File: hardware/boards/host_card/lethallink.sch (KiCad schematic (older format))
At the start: 11 parts, among them J1 PCIe-x4

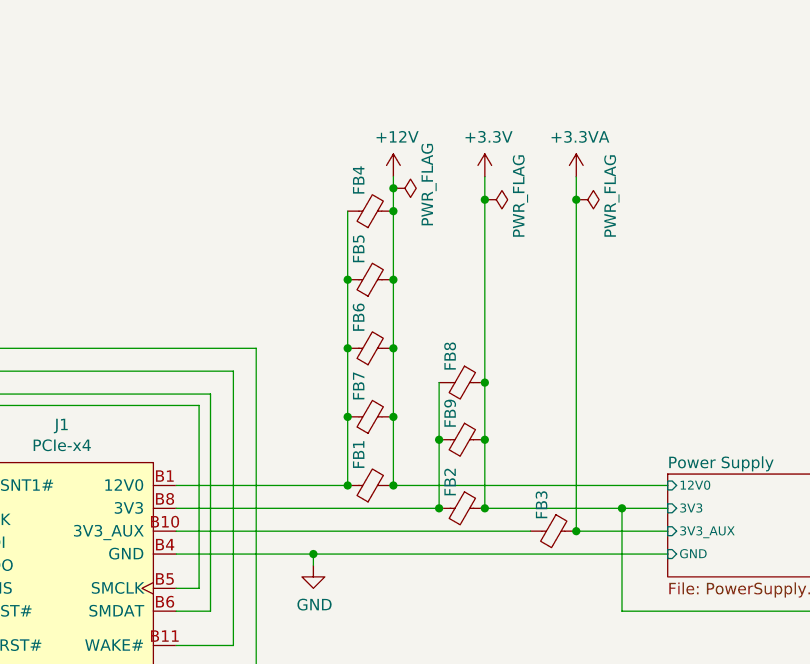
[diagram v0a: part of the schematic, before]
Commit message: Re-routed the PCIe power input side of things to make it not such a massive mess
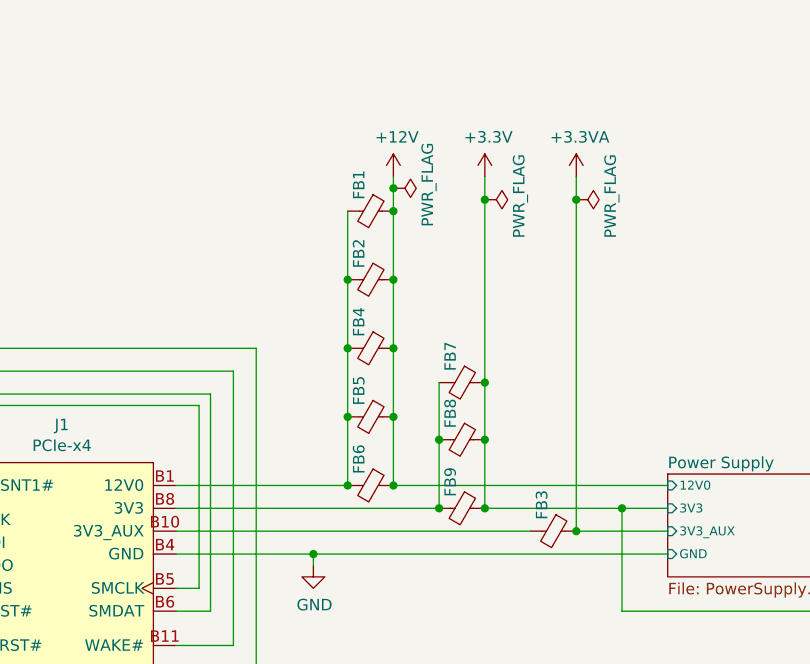
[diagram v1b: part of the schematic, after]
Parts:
- FB1, FB4, FB5, FB6, FB7: value 100 @ 100MHz -> 33 @ 100Mhz; footprint Resistor_SMD:R_0603_1608Metric -> Resistor_SMD:R_0402_1005Metric; MPN BLM18KG101TN1D -> BLM15PX330SN1D
- FB2, FB3, FB8, FB9: value 220 @ 100Mhz -> 33 @ 100Mhz; footprint Resistor_SMD:R_0603_1608Metric -> Resistor_SMD:R_0402_1005Metric; MPN BLM18AG221SN1D -> BLM15PX330SN1D
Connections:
- net +12V: now also FB1.1, FB2.1, FB4.1, FB5.1, FB6.1; no longer FB1.2, FB4.2, FB5.2, FB6.2, FB7.2
- net +3V3: now also FB7.1; no longer FB2.1
- net at FB8.2, FB9.2, J1.A10 (3V3)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: now also FB7.2; no longer FB2.2
- net at J1.A2 (12V0), J1.A3 (12V0), J1.B1 (12V0)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: now also FB1.2, FB2.2, FB4.2, FB5.2, FB6.2; no longer FB1.1, FB4.1, FB5.1, FB6.1, FB7.1
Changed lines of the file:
@@
 Wire Wire Line
 	4300 4350 5850 4350
-Connection ~ 5450 4250
 Wire Wire Line
 	4650 4050 5850 4050
@@
 F7 "VBUS" I R 9000 4050 39
 $EndSheet
-$Comp
-L Device:Ferrite_Bead_Small FB3
-U 1 1 5F57A174
-P 5350 4250
-F 0 "FB3" H 5300 4200 50  0000 R CNN
-F 1 "220 @ 100Mhz" H 5500 4450 50  0001 R CNN
-F 2 "Resistor_SMD:R_0603_1608Metric" V 5280 4250 50  0001 C CNN
-F 3 "~" H 5350 4250 50  0001 C CNN
-F 4 "Murata Electronics" H 5350 4250 50  0001 C CNN "MFR"
-F 5 "BLM18AG221SN1D" H 5350 4250 50  0001 C CNN "MPN"
-	1    5350 4250
-	0    1    1    0
-$EndComp
-$Comp
-L Device:Ferrite_Bead_Small FB2
-U 1 1 5F579DEB
-P 4950 4150
-F 0 "FB2" H 4900 4100 50  0000 R CNN
-F 1 "220 @ 100Mhz" H 5100 4350 50  0001 R CNN
-F 2 "Resistor_SMD:R_0603_1608Metric" V 4880 4150 50  0001 C CNN
-F 3 "~" H 4950 4150 50  0001 C CNN
-F 4 "Murata Electronics" H 4950 4150 50  0001 C CNN "MFR"
-F 5 "BLM18AG221SN1D" H 4950 4150 50  0001 C CNN "MPN"
-	1    4950 4150
-	0    1    1    0
-$EndComp
 Wire Wire Line
 	5650 4150 5850 4150
@@
 Wire Wire Line
 	7000 4050 8350 4050
-$Comp
-L Device:Ferrite_Bead_Small FB1
-U 1 1 5EEA5842
-P 4550 4050
-F 0 "FB1" H 4750 4100 50  0000 R CNN
-F 1 "100 @ 100MHz" H 4700 4250 50  0001 R CNN
-F 2 "Resistor_SMD:R_0603_1608Metric" V 4480 4050 50  0001 C CNN
-F 3 "~" H 4550 4050 50  0001 C CNN
-F 4 "Murata Electronics" H 4550 4050 50  0001 C CNN "MFR"
-F 5 "BLM18KG101TN1D" H 4550 4050 50  0001 C CNN "MPN"
-	1    4550 4050
-	0    -1   -1   0
-$EndComp
 $Sheet
 S 5850 4000 950  450
@@
 $EndComp
 Connection ~ 4300 4350
-$Comp
-L Device:Ferrite_Bead_Small FB9
-U 1 1 5F410C07
-P 4950 3850
-F 0 "FB9" H 4900 3800 50  0000 R CNN
-F 1 "220 @ 100Mhz" H 5100 4050 50  0001 R CNN
-F 2 "Resistor_SMD:R_0603_1608Metric" V 4880 3850 50  0001 C CNN
-F 3 "~" H 4950 3850 50  0001 C CNN
-F 4 "Murata Electronics" H 4950 3850 50  0001 C CNN "MFR"
-F 5 "BLM18AG221SN1D" H 4950 3850 50  0001 C CNN "MPN"
-	1    4950 3850
-	0    1    1    0
-$EndComp
-Connection ~ 5050 3850
-Wire Wire Line
-	5050 3850 5050 4150
-Connection ~ 5050 4150
-$Comp
-L Device:Ferrite_Bead_Small FB8
-U 1 1 5F41D475
-P 4950 3600
-F 0 "FB8" H 4900 3550 50  0000 R CNN
-F 1 "220 @ 100Mhz" H 5100 3800 50  0001 R CNN
-F 2 "Resistor_SMD:R_0603_1608Metric" V 4880 3600 50  0001 C CNN
-F 3 "~" H 4950 3600 50  0001 C CNN
-F 4 "Murata Electronics" H 4950 3600 50  0001 C CNN "MFR"
-F 5 "BLM18AG221SN1D" H 4950 3600 50  0001 C CNN "MPN"
-	1    4950 3600
-	0    1    1    0
-$EndComp
-Connection ~ 5050 3600
-Wire Wire Line
-	5050 3600 5050 3850
 Wire Wire Line
 	5450 2700 5450 2800
-Connection ~ 4650 4050
-$Comp
-L Device:Ferrite_Bead_Small FB7
-U 1 1 5F46A338
-P 4550 3750
-F 0 "FB7" H 4750 3800 50  0000 R CNN
-F 1 "100 @ 100MHz" H 4700 3950 50  0001 R CNN
-F 2 "Resistor_SMD:R_0603_1608Metric" V 4480 3750 50  0001 C CNN
-F 3 "~" H 4550 3750 50  0001 C CNN
-F 4 "Murata Electronics" H 4550 3750 50  0001 C CNN "MFR"
-F 5 "BLM18KG101TN1D" H 4550 3750 50  0001 C CNN "MPN"
-	1    4550 3750
-	0    -1   -1   0
-$EndComp
-Connection ~ 4650 3750
-Wire Wire Line
-	4650 3750 4650 4050
-$Comp
-L Device:Ferrite_Bead_Small FB6
-U 1 1 5F46A91E
-P 4550 3450
-F 0 "FB6" H 4750 3500 50  0000 R CNN
-F 1 "100 @ 100MHz" H 4700 3650 50  0001 R CNN
-F 2 "Resistor_SMD:R_0603_1608Metric" V 4480 3450 50  0001 C CNN
-F 3 "~" H 4550 3450 50  0001 C CNN
-F 4 "Murata Electronics" H 4550 3450 50  0001 C CNN "MFR"
-F 5 "BLM18KG101TN1D" H 4550 3450 50  0001 C CNN "MPN"
-	1    4550 3450
-	0    -1   -1   0
-$EndComp
-Connection ~ 4650 3450
-Wire Wire Line
-	4650 3450 4650 3750
-$Comp
-L Device:Ferrite_Bead_Small FB5
-U 1 1 5F4730D6
-P 4550 3150
-F 0 "FB5" H 4750 3200 50  0000 R CNN
-F 1 "100 @ 100MHz" H 4700 3350 50  0001 R CNN
-F 2 "Resistor_SMD:R_0603_1608Metric" V 4480 3150 50  0001 C CNN
-F 3 "~" H 4550 3150 50  0001 C CNN
-F 4 "Murata Electronics" H 4550 3150 50  0001 C CNN "MFR"
-F 5 "BLM18KG101TN1D" H 4550 3150 50  0001 C CNN "MPN"
-	1    4550 3150
-	0    -1   -1   0
-$EndComp
-Connection ~ 4650 3150
-Wire Wire Line
-	4650 3150 4650 3450
-$Comp
-L Device:Ferrite_Bead_Small FB4
-U 1 1 5F479C67
-P 4550 2850
-F 0 "FB4" H 4750 2900 50  0000 R CNN
-F 1 "100 @ 100MHz" H 4700 3050 50  0001 R CNN
-F 2 "Resistor_SMD:R_0603_1608Metric" V 4480 2850 50  0001 C CNN
-F 3 "~" H 4550 2850 50  0001 C CNN
-F 4 "Murata Electronics" H 4550 2850 50  0001 C CNN "MFR"
-F 5 "BLM18KG101TN1D" H 4550 2850 50  0001 C CNN "MPN"
-	1    4550 2850
-	0    -1   -1   0
-$EndComp
-Connection ~ 4650 2850
-Wire Wire Line
-	4650 2850 4650 3150
-Wire Wire Line
-	4450 2850 4450 3150
-Wire Wire Line
-	4450 3450 4450 3750
-Wire Wire Line
-	4450 3150 4450 3450
-Connection ~ 4450 3150
-Connection ~ 4450 3450
-Wire Wire Line
-	4450 3750 4450 4050
-Connection ~ 4450 3750
-Connection ~ 4450 4050
-Wire Wire Line
-	4850 3600 4850 3850
-Wire Wire Line
-	4850 3850 4850 4150
-Connection ~ 4850 3850
-Connection ~ 4850 4150
 $Comp
 L Device:Ferrite_Bead_Small FB10
@@
 $EndComp
 Connection ~ 4650 2750
-Wire Wire Line
-	4650 2750 4650 2850
 $Comp
 L power:PWR_FLAG #FLG0102
@@
 $EndComp
 Connection ~ 5050 2800
-Wire Wire Line
-	5050 2800 5050 3600
 $Comp
 L power:PWR_FLAG #FLG0103
@@
 Wire Wire Line
 	9900 2700 10050 2700
+Wire Wire Line
+	4450 2850 4450 3150
+Wire Wire Line
+	4650 2750 4650 2850
+Wire Wire Line
+	4850 3600 4850 3850
+Wire Wire Line
+	5050 2800 5050 3600
+Connection ~ 5450 4250
+$Comp
+L Device:Ferrite_Bead_Small FB3
+U 1 1 5F57A174
+P 5350 4250
+F 0 "FB3" H 5300 4200 50  0000 R CNN
+F 1 "33 @ 100Mhz" H 5500 4450 50  0001 R CNN
+F 2 "Resistor_SMD:R_0402_1005Metric" V 5280 4250 50  0001 C CNN
+F 3 "~" H 5350 4250 50  0001 C CNN
+F 4 "Murata Electronics" H 5350 4250 50  0001 C CNN "MFR"
+F 5 "BLM15PX330SN1D" H 5350 4250 50  0001 C CNN "MPN"
+	1    5350 4250
+	0    1    1    0
+$EndComp
+$Comp
+L Device:Ferrite_Bead_Small FB9
+U 1 1 5EFC20C8
+P 4950 4150
+F 0 "FB9" H 4900 4100 50  0000 R CNN
+F 1 "33 @ 100Mhz" H 5100 4350 50  0001 R CNN
+F 2 "Resistor_SMD:R_0402_1005Metric" V 4880 4150 50  0001 C CNN
+F 3 "~" H 4950 4150 50  0001 C CNN
+F 4 "Murata Electronics" H 4950 4150 50  0001 C CNN "MFR"
+F 5 "BLM15PX330SN1D" H 4950 4150 50  0001 C CNN "MPN"
+	1    4950 4150
+	0    1    1    0
+$EndComp
+Connection ~ 5050 4150
+Connection ~ 4850 4150
+$Comp
+L Device:Ferrite_Bead_Small FB7
+U 1 1 5EFC24FC
+P 4950 3600
+F 0 "FB7" H 4900 3550 50  0000 R CNN
+F 1 "33 @ 100Mhz" H 5100 3800 50  0001 R CNN
+F 2 "Resistor_SMD:R_0402_1005Metric" V 4880 3600 50  0001 C CNN
+F 3 "~" H 4950 3600 50  0001 C CNN
+F 4 "Murata Electronics" H 4950 3600 50  0001 C CNN "MFR"
+F 5 "BLM15PX330SN1D" H 4950 3600 50  0001 C CNN "MPN"
+	1    4950 3600
+	0    1    1    0
+$EndComp
+Connection ~ 5050 3600
+Wire Wire Line
+	5050 3600 5050 3850
+$Comp
+L Device:Ferrite_Bead_Small FB8
+U 1 1 5EFC3129
+P 4950 3850
+F 0 "FB8" H 4900 3800 50  0000 R CNN
+F 1 "33 @ 100Mhz" H 5100 4050 50  0001 R CNN
+F 2 "Resistor_SMD:R_0402_1005Metric" V 4880 3850 50  0001 C CNN
+F 3 "~" H 4950 3850 50  0001 C CNN
+F 4 "Murata Electronics" H 4950 3850 50  0001 C CNN "MFR"
+F 5 "BLM15PX330SN1D" H 4950 3850 50  0001 C CNN "MPN"
+	1    4950 3850
+	0    1    1    0
+$EndComp
+Connection ~ 5050 3850
+Wire Wire Line
+	5050 3850 5050 4150
+Connection ~ 4850 3850
+Wire Wire Line
+	4850 3850 4850 4150
+$Comp
+L Device:Ferrite_Bead_Small FB6
+U 1 1 5EFC353B
+P 4550 4050
+F 0 "FB6" H 4500 4000 50  0000 R CNN
+F 1 "33 @ 100Mhz" H 4700 4250 50  0001 R CNN
+F 2 "Resistor_SMD:R_0402_1005Metric" V 4480 4050 50  0001 C CNN
+F 3 "~" H 4550 4050 50  0001 C CNN
+F 4 "Murata Electronics" H 4550 4050 50  0001 C CNN "MFR"
+F 5 "BLM15PX330SN1D" H 4550 4050 50  0001 C CNN "MPN"
+	1    4550 4050
+	0    1    1    0
+$EndComp
+Connection ~ 4650 4050
+Connection ~ 4450 4050
+$Comp
+L Device:Ferrite_Bead_Small FB5
+U 1 1 5EFC39E3
+P 4550 3750
+F 0 "FB5" H 4500 3700 50  0000 R CNN
+F 1 "33 @ 100Mhz" H 4700 3950 50  0001 R CNN
+F 2 "Resistor_SMD:R_0402_1005Metric" V 4480 3750 50  0001 C CNN
+F 3 "~" H 4550 3750 50  0001 C CNN
+F 4 "Murata Electronics" H 4550 3750 50  0001 C CNN "MFR"
+F 5 "BLM15PX330SN1D" H 4550 3750 50  0001 C CNN "MPN"
+	1    4550 3750
+	0    1    1    0
+$EndComp
+Connection ~ 4650 3750
+Wire Wire Line
+	4650 3750 4650 4050
+Connection ~ 4450 3750
+Wire Wire Line
+	4450 3750 4450 4050
+$Comp
+L Device:Ferrite_Bead_Small FB4
+U 1 1 5EFC3DE1
+P 4550 3450
+F 0 "FB4" H 4500 3400 50  0000 R CNN
+F 1 "33 @ 100Mhz" H 4700 3650 50  0001 R CNN
+F 2 "Resistor_SMD:R_0402_1005Metric" V 4480 3450 50  0001 C CNN
+F 3 "~" H 4550 3450 50  0001 C CNN
+F 4 "Murata Electronics" H 4550 3450 50  0001 C CNN "MFR"
+F 5 "BLM15PX330SN1D" H 4550 3450 50  0001 C CNN "MPN"
+	1    4550 3450
+	0    1    1    0
+$EndComp
+Connection ~ 4650 3450
+Wire Wire Line
+	4650 3450 4650 3750
+Connection ~ 4450 3450
+Wire Wire Line
+	4450 3450 4450 3750
+$Comp
+L Device:Ferrite_Bead_Small FB2
+U 1 1 5EFC41A3
+P 4550 3150
+F 0 "FB2" H 4500 3100 50  0000 R CNN
+F 1 "33 @ 100Mhz" H 4700 3350 50  0001 R CNN
+F 2 "Resistor_SMD:R_0402_1005Metric" V 4480 3150 50  0001 C CNN
+F 3 "~" H 4550 3150 50  0001 C CNN
+F 4 "Murata Electronics" H 4550 3150 50  0001 C CNN "MFR"
+F 5 "BLM15PX330SN1D" H 4550 3150 50  0001 C CNN "MPN"
+	1    4550 3150
+	0    1    1    0
+$EndComp
+Connection ~ 4650 3150
+Wire Wire Line
+	4650 3150 4650 3450
+Connection ~ 4450 3150
+Wire Wire Line
+	4450 3150 4450 3450
+$Comp
+L Device:Ferrite_Bead_Small FB1
+U 1 1 5EFC45BE
+P 4550 2850
+F 0 "FB1" H 4500 2800 50  0000 R CNN
+F 1 "33 @ 100Mhz" H 4700 3050 50  0001 R CNN
+F 2 "Resistor_SMD:R_0402_1005Metric" V 4480 2850 50  0001 C CNN
+F 3 "~" H 4550 2850 50  0001 C CNN
+F 4 "Murata Electronics" H 4550 2850 50  0001 C CNN "MFR"
+F 5 "BLM15PX330SN1D" H 4550 2850 50  0001 C CNN "MPN"
+	1    4550 2850
+	0    1    1    0
+$EndComp
+Connection ~ 4650 2850
+Wire Wire Line
+	4650 2850 4650 3150
 $EndSCHEMATC

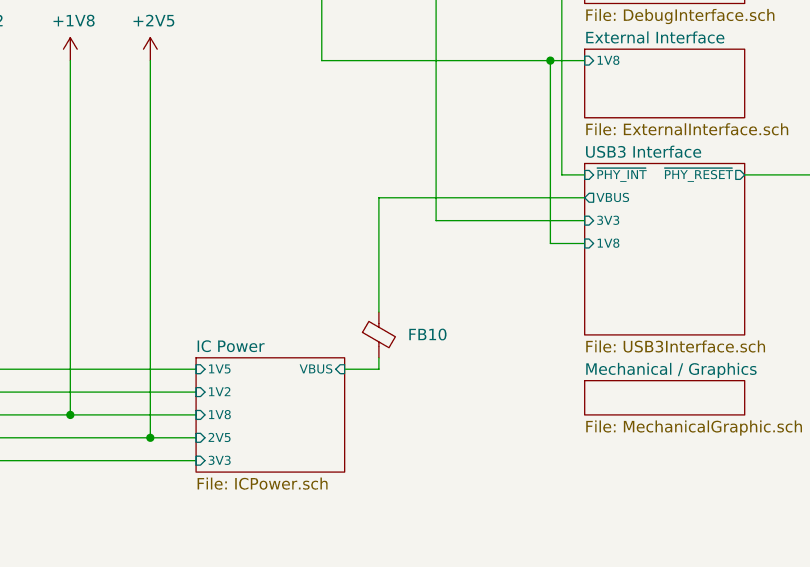
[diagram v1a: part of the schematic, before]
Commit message: Fixed up the consistancy of value naming, 100nF -> 0.1uF. Added the caps for the USB SSRX lines, moved the Ferrite for VBUS to fix a net naming issue
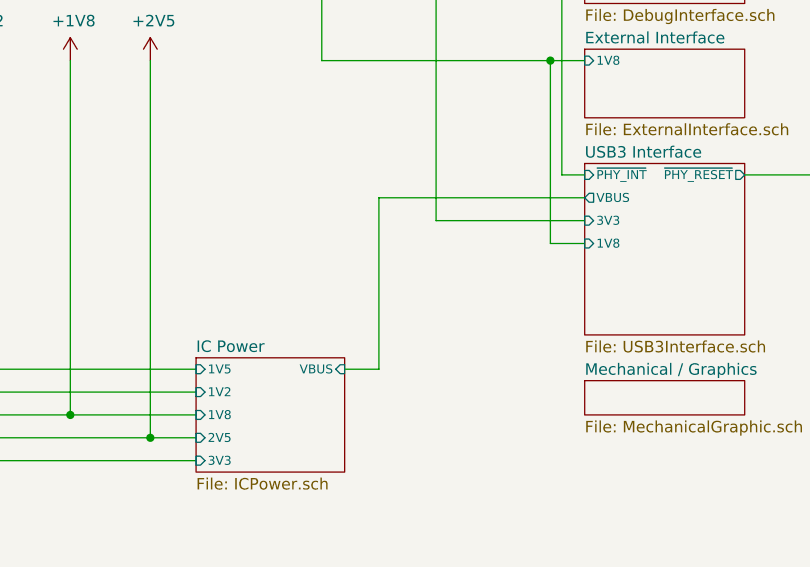
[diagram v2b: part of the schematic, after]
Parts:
- removed FB10: 220 @ 100Mhz, Resistor_SMD:R_0603_1608Metric, symbol Device:Ferrite_Bead_Small
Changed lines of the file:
@@
 Wire Wire Line
 	5450 2700 5450 2800
-$Comp
-L Device:Ferrite_Bead_Small FB10
-U 1 1 5F74D6CA
-P 9150 3900
-F 0 "FB10" H 9450 3900 50  0000 R CNN
-F 1 "220 @ 100Mhz" H 9300 4100 50  0001 R CNN
-F 2 "Resistor_SMD:R_0603_1608Metric" V 9080 3900 50  0001 C CNN
-F 3 "~" H 9150 3900 50  0001 C CNN
-F 4 "Murata Electronics" H 9150 3900 50  0001 C CNN "MFR"
-F 5 "BLM18AG221SN1D" H 9150 3900 50  0001 C CNN "MPN"
-	1    9150 3900
-	1    0    0    -1
-$EndComp
-Wire Wire Line
-	9150 4050 9150 4000
 Wire Wire Line
 	9000 4050 9150 4050
@@
 NoConn ~ 8400 950
 Wire Wire Line
-	9150 3800 9150 3300
-Wire Wire Line
 	9150 3300 10050 3300
 $Sheet
@@
 Wire Wire Line
 	4650 2850 4650 3150
+Wire Wire Line
+	9150 3300 9150 4050
 $EndSCHEMATC

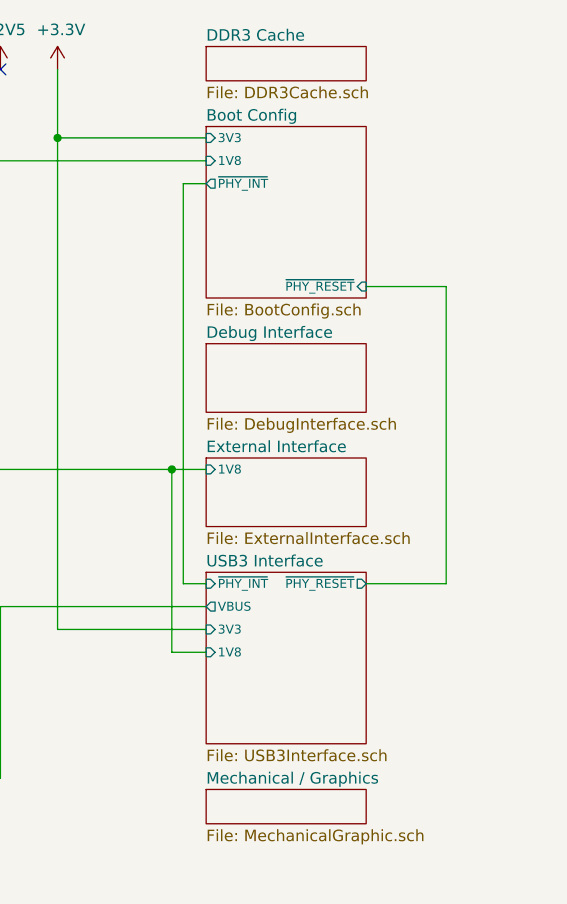
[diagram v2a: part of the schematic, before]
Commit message: Added a pin-header for the FPGA SPI flash lines to allow for the USB PHY to do a DFU update of the gateware when closed
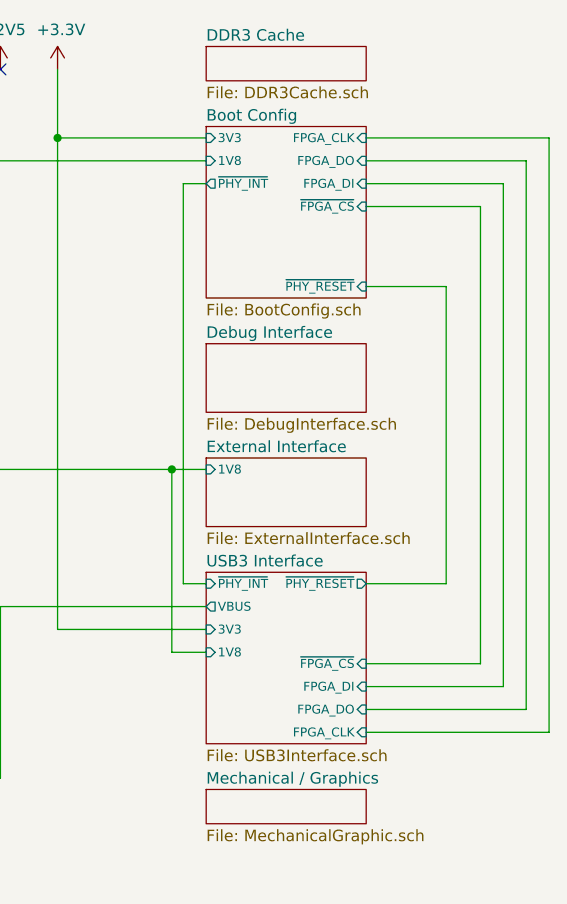
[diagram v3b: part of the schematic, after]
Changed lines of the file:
@@
 F4 "~PHY_INT" O L 10050 1450 39
 F5 "~PHY_RESET" I R 10750 1900 39
+F6 "~FPGA_CS" I R 10750 1550 39
+F7 "FPGA_DO" I R 10750 1350 39
+F8 "FPGA_DI" I R 10750 1450 39
+F9 "FPGA_CLK" I R 10750 1250 39
 $EndSheet
 Wire Wire Line
@@
 F5 "3V3" I L 10050 3400 39
 F6 "1V8" I L 10050 3500 39
+F7 "~FPGA_CS" I R 10750 3550 39
+F8 "FPGA_DO" I R 10750 3750 39
+F9 "FPGA_DI" I R 10750 3650 39
+F10 "FPGA_CLK" I R 10750 3850 39
 $EndSheet
 Wire Wire Line
@@
 Wire Wire Line
 	9150 3300 9150 4050
+Wire Wire Line
+	10750 3550 11250 3550
+Wire Wire Line
+	11250 3550 11250 1550
+Wire Wire Line
+	11250 1550 10750 1550
+Wire Wire Line
+	10750 1450 11350 1450
+Wire Wire Line
+	11350 1450 11350 3650
+Wire Wire Line
+	11350 3650 10750 3650
+Wire Wire Line
+	10750 3750 11450 3750
+Wire Wire Line
+	11450 3750 11450 1350
+Wire Wire Line
+	11450 1350 10750 1350
+Wire Wire Line
+	10750 1250 11550 1250
+Wire Wire Line
+	11550 1250 11550 3850
+Wire Wire Line
+	11550 3850 10750 3850
 $EndSCHEMATC

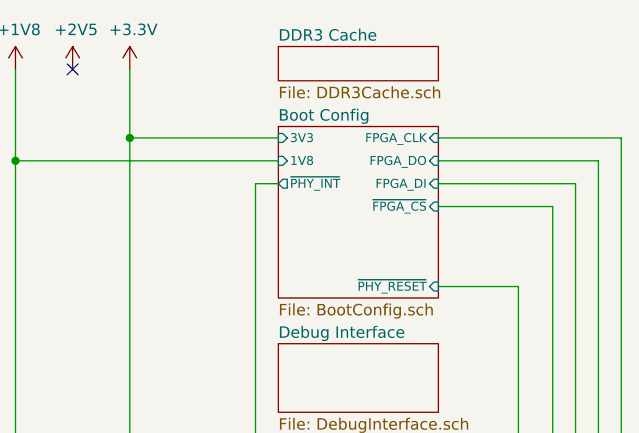
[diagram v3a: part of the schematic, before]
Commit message: Broke out the DDR3 modules and added the 0.75V LDO for the VREFCA and VREFDQ lines for each of the DDR3 modules
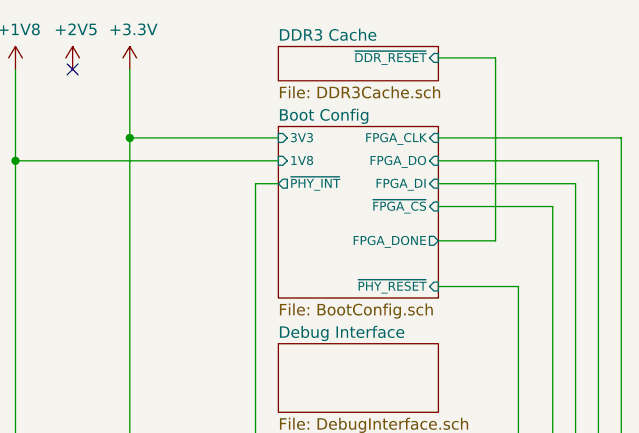
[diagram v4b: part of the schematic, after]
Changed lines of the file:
@@
 F0 "DDR3 Cache" 50
 F1 "DDR3Cache.sch" 50
+F2 "~DDR_RESET" I R 10750 900 39
 $EndSheet
 $Sheet
@@
 F8 "FPGA_DI" I R 10750 1450 39
 F9 "FPGA_CLK" I R 10750 1250 39
+F10 "FPGA_DONE" O R 10750 1700 39
 $EndSheet
 Wire Wire Line
@@
 Wire Wire Line
 	11550 3850 10750 3850
+Wire Wire Line
+	10750 1700 11000 1700
+Wire Wire Line
+	11000 1700 11000 900
+Wire Wire Line
+	11000 900  10750 900
 $EndSCHEMATC
